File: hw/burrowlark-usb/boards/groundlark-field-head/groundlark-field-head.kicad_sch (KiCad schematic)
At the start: 0 parts

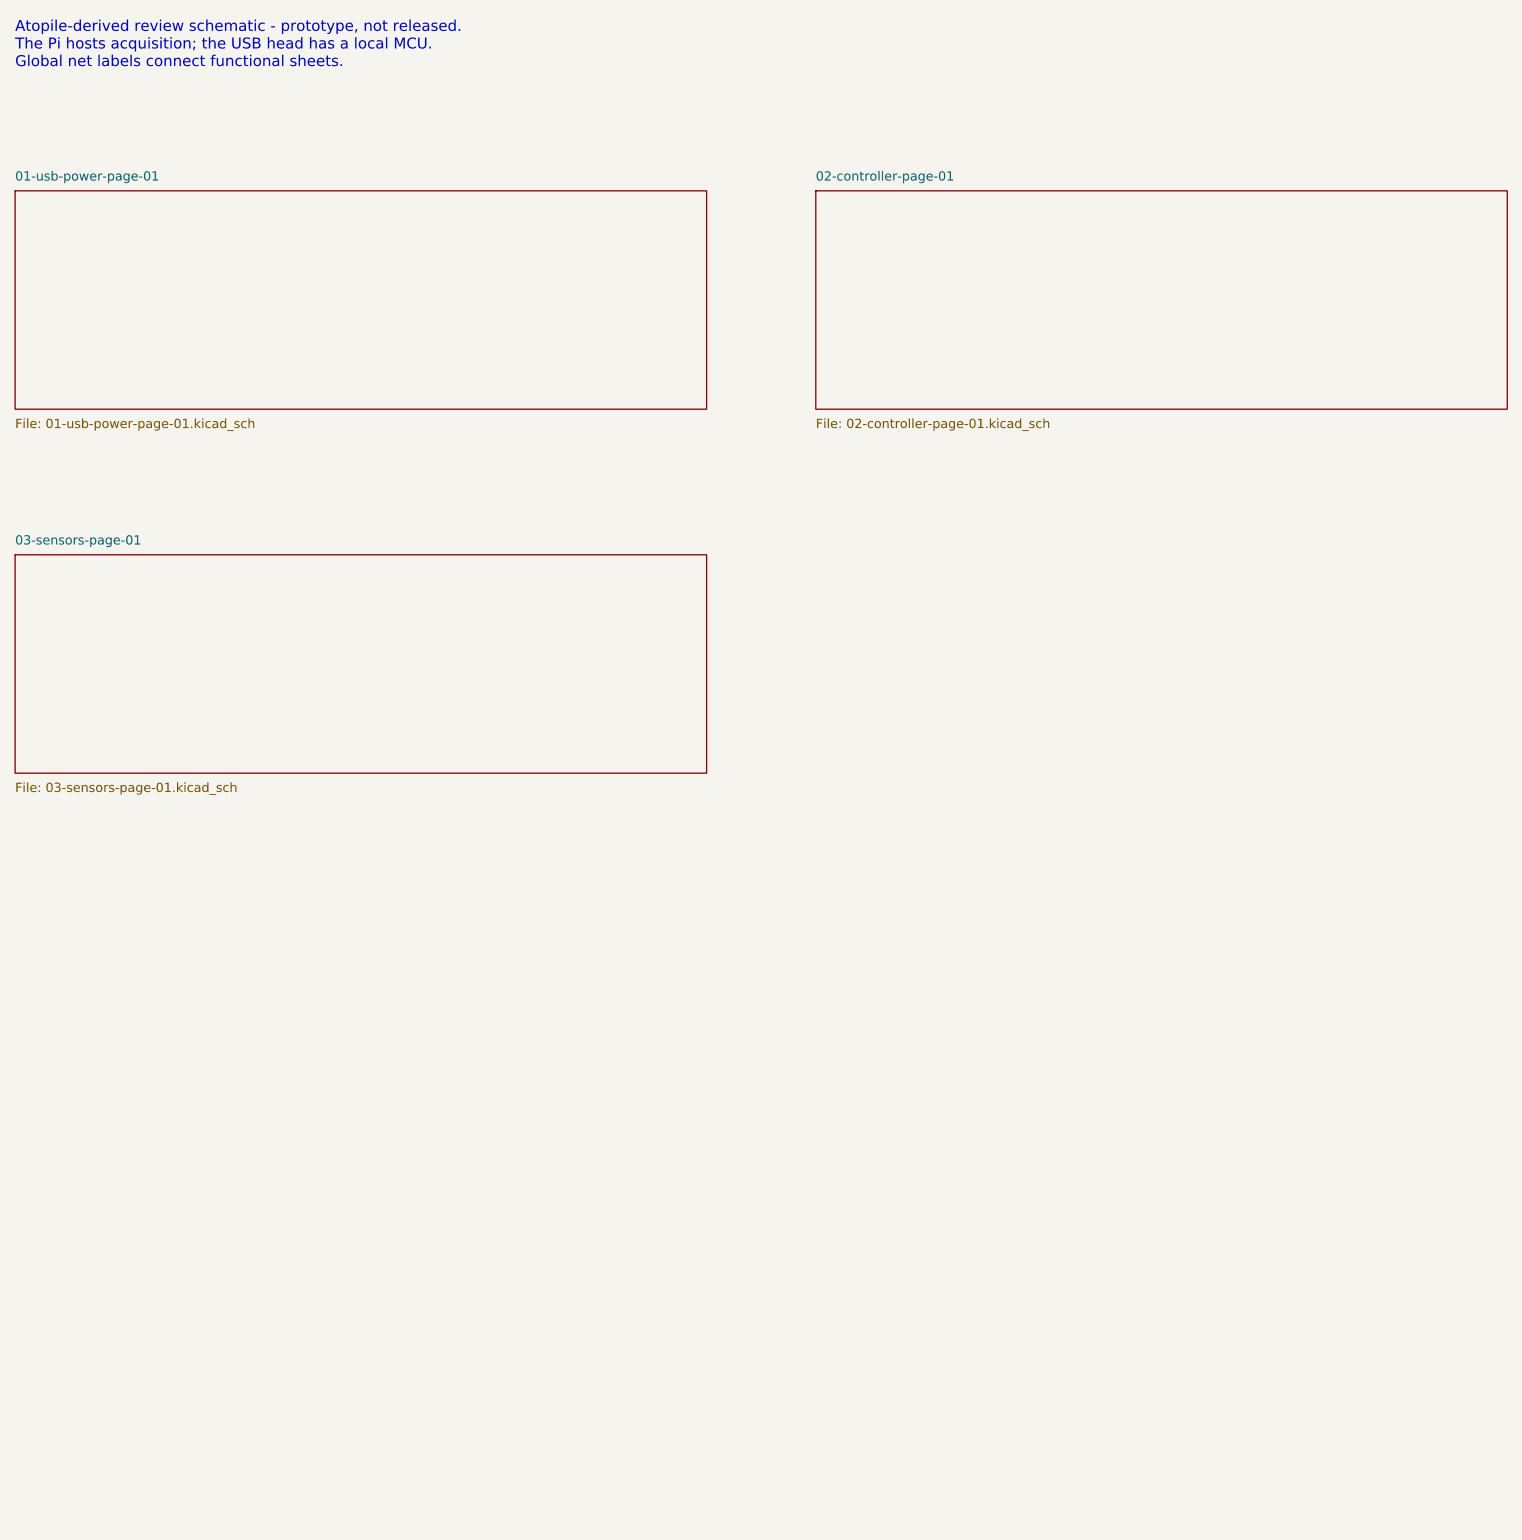
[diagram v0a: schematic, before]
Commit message: Implement Burrowlark B1 four-sensor magnetic array
Use four aligned RM3100 modules on a 30 mm grid with a common SPI trigger, independent data/DRDY lanes and preserved raw cohort timing. Add explicit calibrated averaging, quartet backpressure handling, firmware fault fixtures and the matching workbench/README model.

Keep physical USB, timing, cross-talk and noise qualification explicit. The full-suite DAQHAT assembly failures are reproduced on the unchanged baseline.
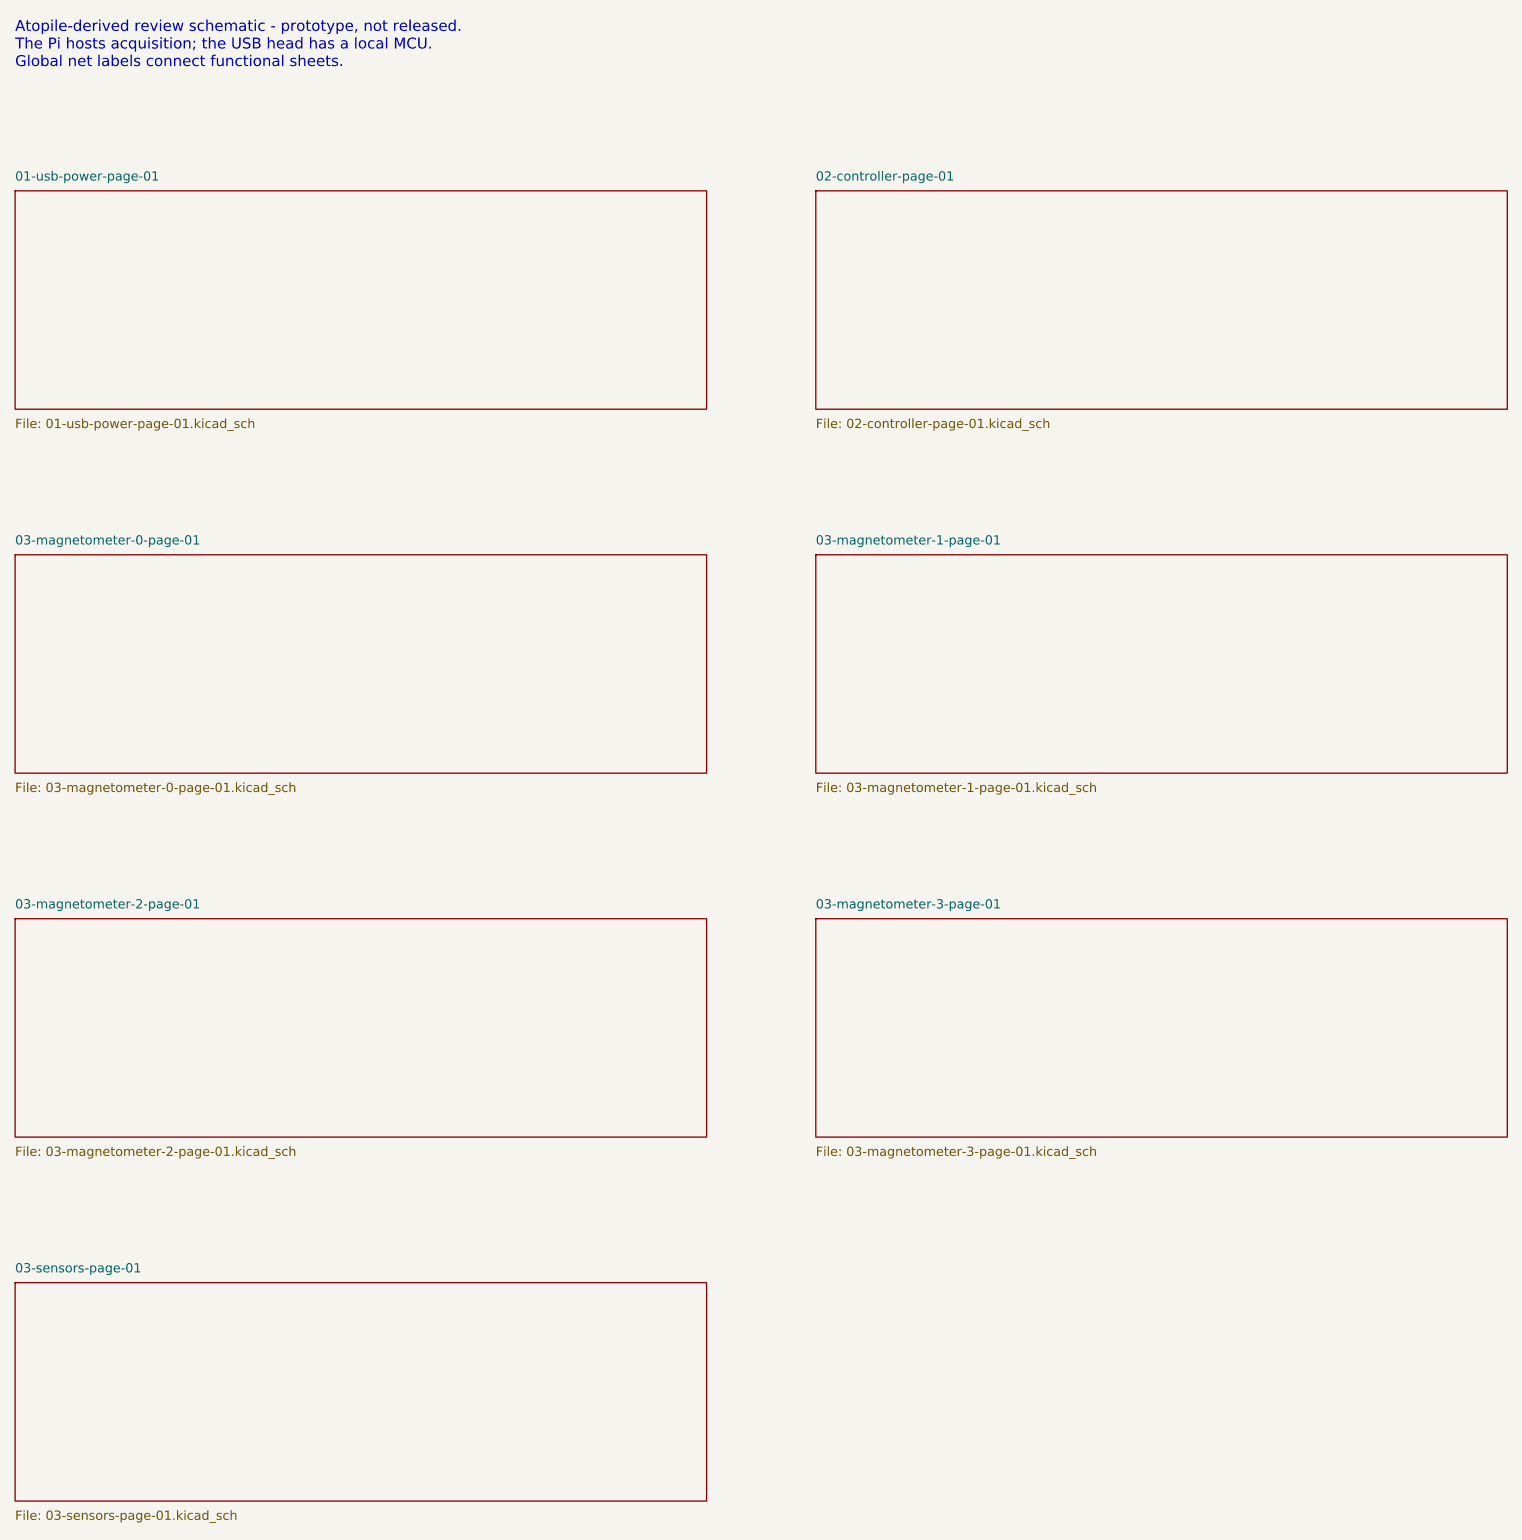
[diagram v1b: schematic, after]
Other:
- added sheet 03-magnetometer-0-page-01 (03-magnetometer-0-page-01.kicad_sch)
- added sheet 03-magnetometer-1-page-01 (03-magnetometer-1-page-01.kicad_sch)
- added sheet 03-magnetometer-2-page-01 (03-magnetometer-2-page-01.kicad_sch)
- added sheet 03-magnetometer-3-page-01 (03-magnetometer-3-page-01.kicad_sch)
